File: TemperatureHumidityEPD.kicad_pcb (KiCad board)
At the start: 4 copper layers, 48 x 43 mm, 66 parts, among them J1 Conn_01x02, J2 FTSH-105-01-L-DV-K, J3 Conn_01x08, J4 Conn_01x24, Q1 Si1308EDL, Q2 IRLML6344, SW1 SW_Push, U1 SI7021, U2 MAX32660GTP, U3 MAX20343H, Y1 32.7680KHZ

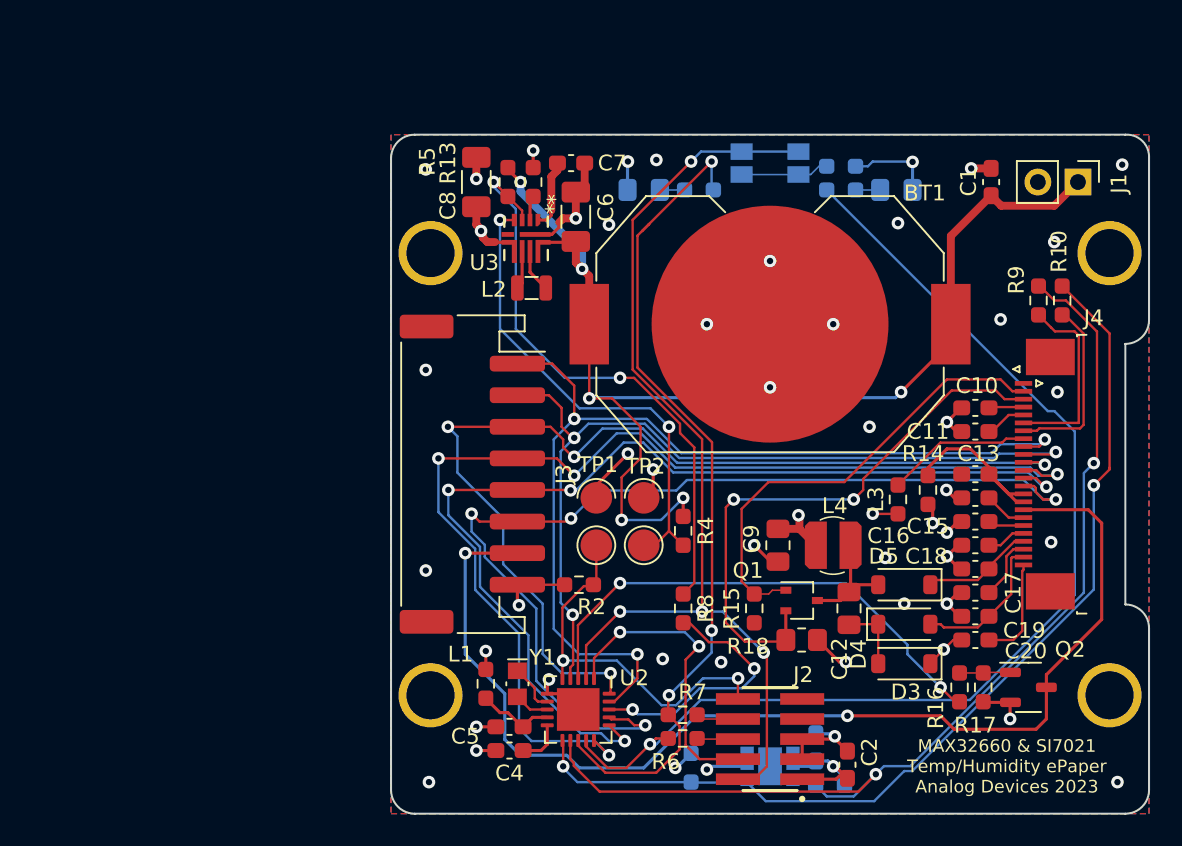
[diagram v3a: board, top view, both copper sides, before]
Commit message: Reversed D1 polarity in schematic and PCB. Moved INGOOD pull-up to 3V3 from input net +BATT. Update version and date.
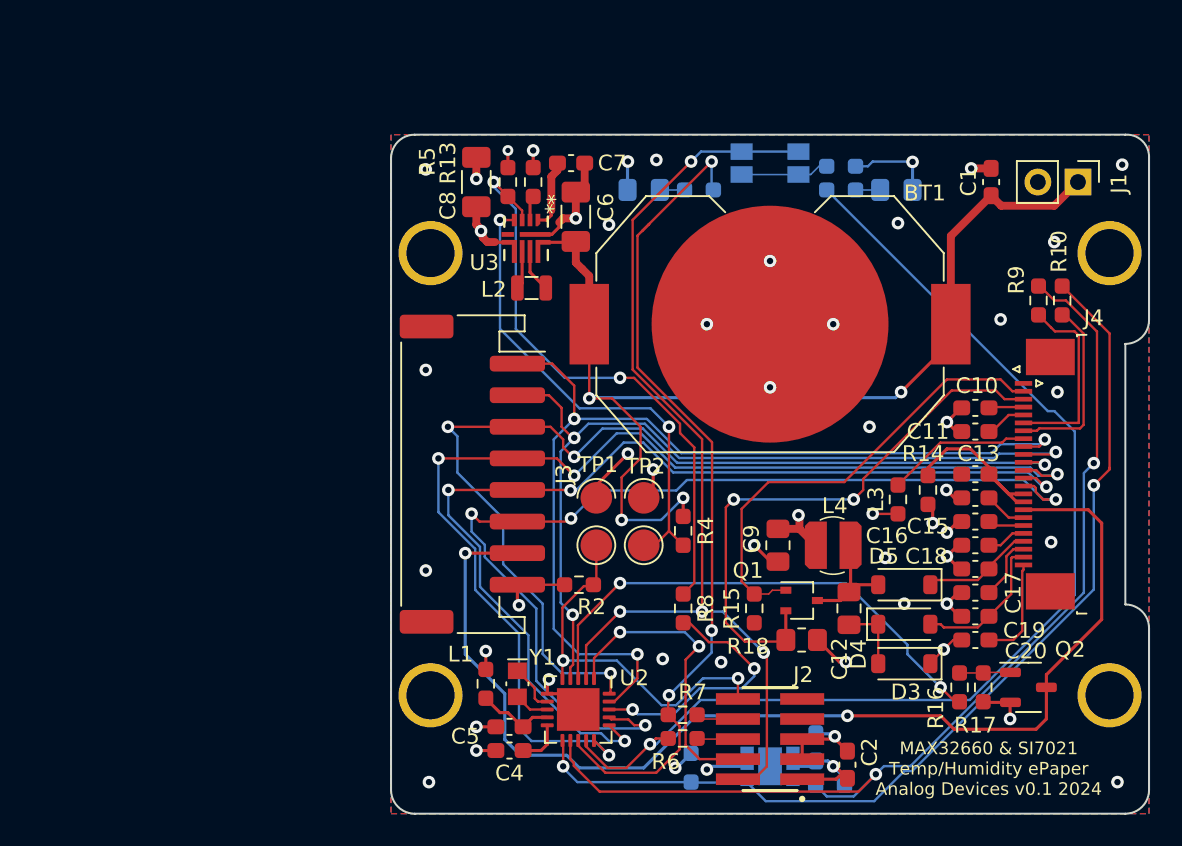
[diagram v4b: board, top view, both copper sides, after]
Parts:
- turned D1 to 0 degrees
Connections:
- D1 pad 1: +3V3 -> Net-(D1-K)
- D1 pad 2: Net-(D1-A) -> +3V3
- R11 pad 2: Net-(D1-A) -> Net-(D1-K)
- R5 pad 1: +BATT -> +3V3
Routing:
- net +BATT: track 77.8 -> 69.4 mm, vias 6 -> 4
- net Net-(D1-K): track 0.00 -> 1.56 mm
- net Net-(D1-A): track 1.56 -> 0.00 mm
- net +3V3: track 32.2 -> 33.3 mm, vias 9 -> 10
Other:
- board text added: "MAX32660 & SI7021 Temp/Humidity ePaper Analog Devices v0.1 2024"
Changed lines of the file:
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@@
   (net 55 "unconnected-(J2-Pin_9-Pad09)")
   (net 56 "Net-(R19-Pad2)")
-  (net 57 "Net-(D1-A)")
+  (net 57 "Net-(D1-K)")
   (net 58 "/EPD_VDD")
   (footprint "Connectors_Custom:BatteryHolder_TE_BATT-HLD-000_1x2032" (layer "F.Cu")
@@
       (stroke (width 0.1) (type solid)) (layer "F.Fab"))
     (pad "1" smd roundrect (at -0.9125 0 270) (size 0.975 0.95) (layers "F.Cu" "F.Paste" "F.Mask") (roundrect_rratio 0.25)
-      (net 6 "+BATT") (pintype "passive"))
+      (net 1 "+3V3") (pintype "passive"))
     (pad "2" smd roundrect (at 0.9125 0 270) (size 0.975 0.95) (layers "F.Cu" "F.Paste" "F.Mask") (roundrect_rratio 0.25)
       (net 40 "Net-(U3-INGOOD)") (pintype "passive"))
@@
     (descr "Resistor SMD 0603 (1608 Metric), square (rectangular) end terminal, IPC_7351 nominal with elongated pad for handsoldering. (Body size source: IPC-SM-782 page 72, https://www.pcb-3d.com/wordpress/wp-content/uploads/ipc-sm-782a_amendment_1_and_2.pdf), generated with kicad-footprint-generator")
     (tags "resistor handsolder")
-    (property "Description" "resistor, 0, 0.25W, thick film, SMT, 0603 (1608)")
-    (property "Part Number" "RCS06030000Z0EC")
+    (property "Description" "resistor, 1k, 0.1W, thin film, 1%, 50ppm, SMT, 0603 (1608)")
+    (property "Part Number" "RT0603FRE131KL")
     (property "Sheetfile" "TemperatureHumidityEPD.kicad_sch")
     (property "Sheetname" "")
@@
     (property "Sheetname" "")
     (attr smd)
-    (fp_text reference "C16" (at 5.5 0.6) (layer "F.SilkS")
+    (fp_text reference "C16" (at 5.6 0.6) (layer "F.SilkS")
         (effects (font (size 1 1) (thickness 0.15)))
     )
@@
     (descr "Resistor SMD 0603 (1608 Metric), square (rectangular) end terminal, IPC_7351 nominal with elongated pad for handsoldering. (Body size source: IPC-SM-782 page 72, https://www.pcb-3d.com/wordpress/wp-content/uploads/ipc-sm-782a_amendment_1_and_2.pdf), generated with kicad-footprint-generator")
     (tags "resistor handsolder")
-    (property "Description" "resistor, 0, 0.25W, thick film, SMT, 0603 (1608)")
-    (property "Part Number" "RCS06030000Z0EC")
+    (property "Description" "resistor, 1k, 0.1W, thin film, 1%, 50ppm, SMT, 0603 (1608)")
+    (property "Part Number" "RT0603FRE131KL")
     (property "Sheetfile" "TemperatureHumidityEPD.kicad_sch")
     (property "Sheetname" "")
@@
       (net 42 "/UART1_TX") (pintype "passive"))
     (pad "2" smd roundrect (at 0.9125 0) (size 0.975 0.95) (layers "B.Cu" "B.Paste" "B.Mask") (roundrect_rratio 0.25)
-      (net 57 "Net-(D1-A)") (pintype "passive"))
+      (net 57 "Net-(D1-K)") (pintype "passive"))
     (model "${KICAD6_3DMODEL_DIR}/Resistor_SMD.3dshapes/R_0603_1608Metric.wrl"
       (offset (xyz 0 0 0))
@@
   )
   (footprint "LED_SMD:LED_0805_2012Metric_Pad1.15x1.40mm_HandSolder" (layer "B.Cu")
-    (at 154.7 89.9 180)
+    (at 154.7 89.9)
     (descr "LED SMD 0805 (2012 Metric), square (rectangular) end terminal, IPC_7351 nominal, (Body size source: https://docs.google.com/spreadsheets/d/1BsfQQcO9C6DZCsRaXUlFlo91Tg2WpOkGARC1WS5S8t0/edit?usp=sharing), generated with kicad-footprint-generator")
     (tags "LED handsolder")
@@
     (property "ki_keywords" "LED diode")
     (attr smd)
-    (fp_text reference "D1" (at 0 1.65) (layer "B.SilkS")
+    (fp_text reference "D1" (at -0.55 -1.75) (layer "B.SilkS")
         (effects (font (size 1 1) (thickness 0.15)) (justify mirror))
     )
@@
     (fp_line (start 1 0.6) (end -0.7 0.6)
       (stroke (width 0.1) (type solid)) (layer "B.Fab"))
-    (pad "1" smd roundrect (at -1.025 0 180) (size 1.15 1.4) (layers "B.Cu" "B.Paste" "B.Mask") (roundrect_rratio 0.2173913043)
-      (net 1 "+3V3") (pinfunction "K") (pintype "passive"))
-    (pad "2" smd roundrect (at 1.025 0 180) (size 1.15 1.4) (layers "B.Cu" "B.Paste" "B.Mask") (roundrect_rratio 0.2173913043)
-      (net 57 "Net-(D1-A)") (pinfunction "A") (pintype "passive"))
+    (pad "1" smd roundrect (at -1.025 0) (size 1.15 1.4) (layers "B.Cu" "B.Paste" "B.Mask") (roundrect_rratio 0.2173913043)
+      (net 57 "Net-(D1-K)") (pinfunction "K") (pintype "passive"))
+    (pad "2" smd roundrect (at 1.025 0) (size 1.15 1.4) (layers "B.Cu" "B.Paste" "B.Mask") (roundrect_rratio 0.2173913043)
+      (net 1 "+3V3") (pinfunction "A") (pintype "passive"))
     (model "${KICAD6_3DMODEL_DIR}/LED_SMD.3dshapes/LED_0805_2012Metric.wrl"
       (offset (xyz 0 0 0))
@@
     (effects (font (size 0.8 0.8) (thickness 0.127)) (justify mirror))
   )
-  (gr_text "Raw ePaper Screen\nAdhere here" (at 150.45 106.9) (layer "B.SilkS")
-    (effects (font (size 0.6 0.6) (thickness 0.127) bold) (justify left mirror))
+  (gr_text "Raw ePaper Screen\nAdhere here" (at 154 107.15) (layer "B.SilkS")
+    (effects (font (size 1 1) (thickness 0.127) bold) (justify left mirror))
   )
-  (gr_text "MAX32660 & SI7021 \nTemp/Humidity ePaper\nAnalog Devices 2023" (at 161.7 126.4) (layer "F.SilkS")
+  (gr_text "MAX32660 & SI7021 \nTemp/Humidity ePaper\nAnalog Devices v0.1 2024" (at 160.55 126.55) (layer "F.SilkS")
     (effects (font (size 0.8 0.8) (thickness 0.127)))
   )
@@
   (segment (start 129.3065 93.2175) (end 130.0875 93.2175) (width 0.2) (layer "F.Cu") (net 1))
   (segment (start 128.1 90.9625) (end 128.1 92.1) (width 0.5) (layer "F.Cu") (net 1))
+  (segment (start 130.1 88.4875) (end 130.1 87.4) (width 0.2) (layer "F.Cu") (net 1))
   (segment (start 128.1 92.1) (end 128.4 92.4) (width 0.5) (layer "F.Cu") (net 1))
   (segment (start 148.5625 111.3625) (end 148.5625 110.5625) (width 0.5) (layer "F.Cu") (net 1))
@@
   (via (at 128.7 119.1) (size 0.8) (drill 0.4) (layers "F.Cu" "B.Cu") (free) (net 1))
   (via (at 157 111) (size 0.8) (drill 0.4) (layers "F.Cu" "B.Cu") (free) (net 1))
+  (via (at 130.1 87.4) (size 0.6858) (drill 0.3302) (layers "F.Cu" "B.Cu") (net 1))
   (via (at 150.7 126.4) (size 0.8) (drill 0.4) (layers "F.Cu" "B.Cu") (net 1))
   (segment (start 152.9 88.4) (end 153.2 88.1) (width 0.1524) (layer "B.Cu") (net 1))
@@
   (segment (start 151.5 114.8) (end 155.4 118.7) (width 0.1524) (layer "B.Cu") (net 5))
   (segment (start 138.5 104.9) (end 136.7 103.1) (width 0.1524) (layer "F.Cu") (net 6))
-  (segment (start 130.1 88.4875) (end 130.1 88.6) (width 0.2) (layer "F.Cu") (net 6))
   (segment (start 137.3 110.8) (end 137.3 108.1) (width 0.1524) (layer "F.Cu") (net 6))
-  (segment (start 130.1 88.6) (end 130.9 89.4) (width 0.2) (layer "F.Cu") (net 6))
   (segment (start 158.15 98.4) (end 158.15 99.55) (width 0.2) (layer "F.Cu") (net 6))
   (segment (start 141.2 110.575) (end 141.2 109.4) (width 0.2) (layer "F.Cu") (net 6))
@@
   (segment (start 135.25 95.35) (end 134.8 94.9) (width 0.5) (layer "F.Cu") (net 6))
   (via (at 155 102.7) (size 0.8) (drill 0.4) (layers "F.Cu" "B.Cu") (net 6))
-  (via (at 134.8 94.9) (size 0.8) (drill 0.4) (layers "F.Cu" "B.Cu") (net 6))
   (via (at 135.25 103.1) (size 0.8) (drill 0.4) (layers "F.Cu" "B.Cu") (net 6))
-  (via (at 130.9 89.4) (size 0.8) (drill 0.4) (layers "F.Cu" "B.Cu") (net 6))
   (via (at 141.2 109.4) (size 0.8) (drill 0.4) (layers "F.Cu" "B.Cu") (net 6))
   (via (at 137.3 110.8) (size 0.8) (drill 0.4) (layers "F.Cu" "B.Cu") (net 6))
   (segment (start 139.8 110.8) (end 141.2 109.4) (width 0.1524) (layer "B.Cu") (net 6))
-  (segment (start 134.8 94.9) (end 134.8 93.9) (width 0.5) (layer "B.Cu") (net 6))
   (segment (start 135.2976 103.0524) (end 135.25 103.1) (width 0.2) (layer "B.Cu") (net 6))
   (segment (start 155 102.7) (end 154.6476 103.0524) (width 0.2) (layer "B.Cu") (net 6))
-  (segment (start 134.8 93.9) (end 130.9 90) (width 0.5) (layer "B.Cu") (net 6))
   (segment (start 137.3 110.8) (end 139.8 110.8) (width 0.1524) (layer "B.Cu") (net 6))
-  (segment (start 130.9 90) (end 130.9 89.4) (width 0.5) (layer "B.Cu") (net 6))
   (segment (start 154.6476 103.0524) (end 135.2976 103.0524) (width 0.2) (layer "B.Cu") (net 6))
   (segment (start 132.6 125) (end 132.2 125.4) (width 0.2) (layer "F.Cu") (net 7))
